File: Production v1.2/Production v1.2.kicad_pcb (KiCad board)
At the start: 2 copper layers, 35 x 31.2 mm, 39 parts, among them IC1 MAX3323EEUE+T, IC2 AP7375-33SA-7, J1 530480510, J13 FH34SRJ-16S-0.5SH_50_, J2 530480410, J3 USB4085-GF-A_REVB, U2 ADR02AUJZ-REEL7, U3 ATSAMD21G18A-AUT, Y1 ECS-.327-12.5-1210-TR

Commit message: 1.2 routed
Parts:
- removed 3V3, GND, SWCLK, SWDIO: TestPoint_Pad_D1.5mm, TestPoint:TestPoint_Pad_D1.5mm
- removed D4: LED, LED_SMD:LED_0805_2012Metric
- removed J13: FH34SRJ-16S-0.5SH_50_, FH34SRJ_16S_0_5SH_50:HRS_FH34SRJ-16S-0.5SH_50_
- added C14: 10uF, Capacitor_SMD:C_0402_1005Metric, B.Cu at (117.9, 89.2)
- added C15: 100nF, Capacitor_SMD:C_0402_1005Metric, B.Cu at (118.2, 85.7)
- added C16: 10uF, Capacitor_SMD:C_0402_1005Metric, B.Cu at (98.3, 82.2)
- added C17: 100nF, Capacitor_SMD:C_0402_1005Metric, B.Cu at (98.3, 84.1)
- added C18: 22uF,10V+, Capacitor_SMD:C_0402_1005Metric, B.Cu at (117.9, 87.4)
- added C19: 4.7uF, Capacitor_SMD:C_0402_1005Metric, B.Cu at (99.6, 83.3)
- added C20: 100nF, Capacitor_SMD:C_0402_1005Metric, B.Cu at (99.6, 85.2)
- added C21: 100nF, Capacitor_SMD:C_0402_1005Metric, B.Cu at (99.6, 84.3)
- added C22: .1uF, 10v+, Capacitor_SMD:C_0402_1005Metric, B.Cu at (92.5, 92.6)
- added C23: .1uF, 50V, Capacitor_SMD:C_0805_2012Metric, B.Cu at (95.3, 93.0)
- added C24: .1uF, 10v+, Capacitor_SMD:C_0402_1005Metric, B.Cu at (96.3, 86.5)
- added C25: .1uF, 50V, Capacitor_SMD:C_0805_2012Metric, B.Cu at (97.8, 90.9)
- added D3: D_Schottky, Diode_SMD:D_1206_3216Metric, B.Cu at (120.8, 92.3)
- added J4: FH34SRJ-16S-0.5SH_50_, FH34SRJ_16S_0_5SH_50:HRS_FH34SRJ-16S-0.5SH_50_, F.Cu at (106.5, 73.7)
- added L1: BLM15AX601SN1D, digikey-footprints:0603, B.Cu at (99.3, 81.2)
- added L2: BLM15AX601SN1D, digikey-footprints:0603, B.Cu at (100.6, 81.2)
- added R4: 5K6, Resistor_SMD:R_0201_0603Metric, B.Cu at (102.7, 88.2)
- added U1: ATSAMD21G18A-AUT, Package_QFP:TQFP-48_7x7mm_P0.5mm, B.Cu at (106.6, 81.8)
- C10, C11, C12, C9: moved to F.Cu
- C13: value 22uF,10V+ -> 2.2uF,50V+; footprint Capacitor_SMD:C_0402_1005Metric -> Capacitor_SMD:C_0805_2012Metric
- C4: value 2.2uF,100V -> 100nF,25V; footprint Capacitor_SMD:C_0805_2012Metric -> Capacitor_SMD:C_0402_1005Metric
- C5: value 100nF,25V -> 22pF
- C7: value 22pF -> 100nF
- C8: moved to B.Cu
- D1: value D_Schottky -> LED; footprint Diode_SMD:D_1206_3216Metric -> LED_SMD:LED_0805_2012Metric; moved to F.Cu
- R3: value 4K7 -> 65; moved to F.Cu
- R6: value 5K1 -> 1K
- R7: value 680K -> 5K1; moved to F.Cu
- R8: value 65 -> 680K
- U3: value ATSAMD21G18A-AUT -> ADR06BUJZ-REEL7; footprint Package_QFP:TQFP-48_7x7mm_P0.5mm -> Package_TO_SOT_SMD:TSOT-23-5
- moved D1 29.5 mm to (100.3, 69.1), turned to -90 degrees
- moved R6 17.4 mm to (105.7, 87.3)
- moved C7 15.1 mm to (111.0, 86.0), turned to -90 degrees
- moved U3 12.2 mm to (98.5, 88.0), turned to 90 degrees
- moved R5 11.2 mm to (104.3, 88.2), turned to 0 degrees
- moved Y1 11.2 mm to (101.6, 85.9), turned to 0 degrees
- moved C6 10.8 mm to (101.0, 84.0), turned to -90 degrees
- moved C5 10.8 mm to (103.0, 86.5), turned to 90 degrees
- moved C8 9.28 mm to (106.0, 88.2), turned to 180 degrees
- moved S1 8.73 mm to (90.7, 71.5), turned to 0 degrees
- moved C11 8.08 mm to (102.5, 76.6), turned to 180 degrees
- moved R7 7.76 mm to (112.5, 72.0)
- moved C4 7.29 mm to (112.8, 92.5)
- moved R3 6.86 mm to (99.9, 72.2)
- moved C13 6.84 mm to (119.0, 92.2)
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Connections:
- C13 pad 2: +3V3 -> VIN
- C4 pad 1: GND -> /Net-(IC1-V-)
- C4 pad 2: VIN -> GND
- C5 pad 1: /Net-(IC1-V-) -> GND
- C5 pad 2: GND -> Net-(U1-PA00)
- C6 pad 2: Net-(U3-PA00) -> Net-(U1-PA01)
- C7 pad 1: GND -> +3V3
- C7 pad 2: Net-(U3-PA01) -> GND
- C8 pad 1: Net-(U3-VDDCORE) -> VDDCORE
- D1 pad 1: VIN -> GND
- D1 pad 2: VUSB -> Net-(D1-A)
- D2 pad 2: +24V -> VUSB
- R3 pad 1: ZOOM -> SETLED
- R3 pad 2: ZSIG -> Net-(D1-A)
- R5 pad 2: GND -> GNDANA
- R6 pad 1: GND -> SWCLK
- R6 pad 2: OLED_RST -> +3V3
- R7 pad 2: Net-(J13-Pad4) -> OLED_RST
- R8 pad 1: SETLED -> GND
- U2 pad 2: GND -> GNDANA
- U2 pad 3: +24V -> VIN
- U3 pad 1: Net-(U3-PA00) -> unconnected-(U3-TEMP-Pad1)
- U3 pad 2: Net-(U3-PA01) -> GNDANA
- U3 pad 3: SETBTN -> VIN
- U3 pad 4: unconnected-(U3-PA03-Pad4) -> AREFA
- U3 pad 5: GND -> unconnected-(U3-TRIM-Pad5)
- Y1 pad 1: Net-(U3-PA01) -> Net-(U1-PA01)
- Y1 pad 2: Net-(U3-PA00) -> Net-(U1-PA00)
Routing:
- net VIN: track 0.00 -> 35.8 mm, vias 0 -> 2
- net GND: track 32.2 -> 0.00 mm, vias 23 -> 0
- net +3V3: track 33.0 -> 49.8 mm, vias 2 -> 1
- net AREFA: track 0.00 -> 13.3 mm
- net VUSB: track 24.8 -> 14.1 mm, vias 1 -> 0
- net SWCLK: track 11.4 -> 1.41 mm, vias 1 -> 0
- net SWDIO: track 9.92 -> 0.00 mm, vias 1 -> 0
- net SETBTN: track 8.41 -> 17.8 mm
- net VDDANA: track 0.00 -> 6.66 mm
- net SETLED: track 4.55 -> 10.3 mm
- net Net-(U3-PA00): track 4.92 -> 0.00 mm
- net OLED_RST: track 6.17 -> 10.9 mm, vias 2 -> 1
- net ZOOM: track 17.1 -> 12.5 mm
- net Net-(U3-PA01): track 4.04 -> 0.00 mm
- net D-: track 7.87 -> 11.9 mm, vias 0 -> 1
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- added copper zone on B.Cu, net GNDANA
- removed copper zone on B.Cu, net +3V3
- removed copper zone on B.Cu, net GND
- removed copper zone on F.Cu, net GND
- removed copper zone on B.Cu, net VIN
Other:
- outline, holes or cut-outs redrawn
- board text added: "MFSerial v1.2 Max Batchelder"
- board text removed: "MFSerial v1.1 Max Batchelder"

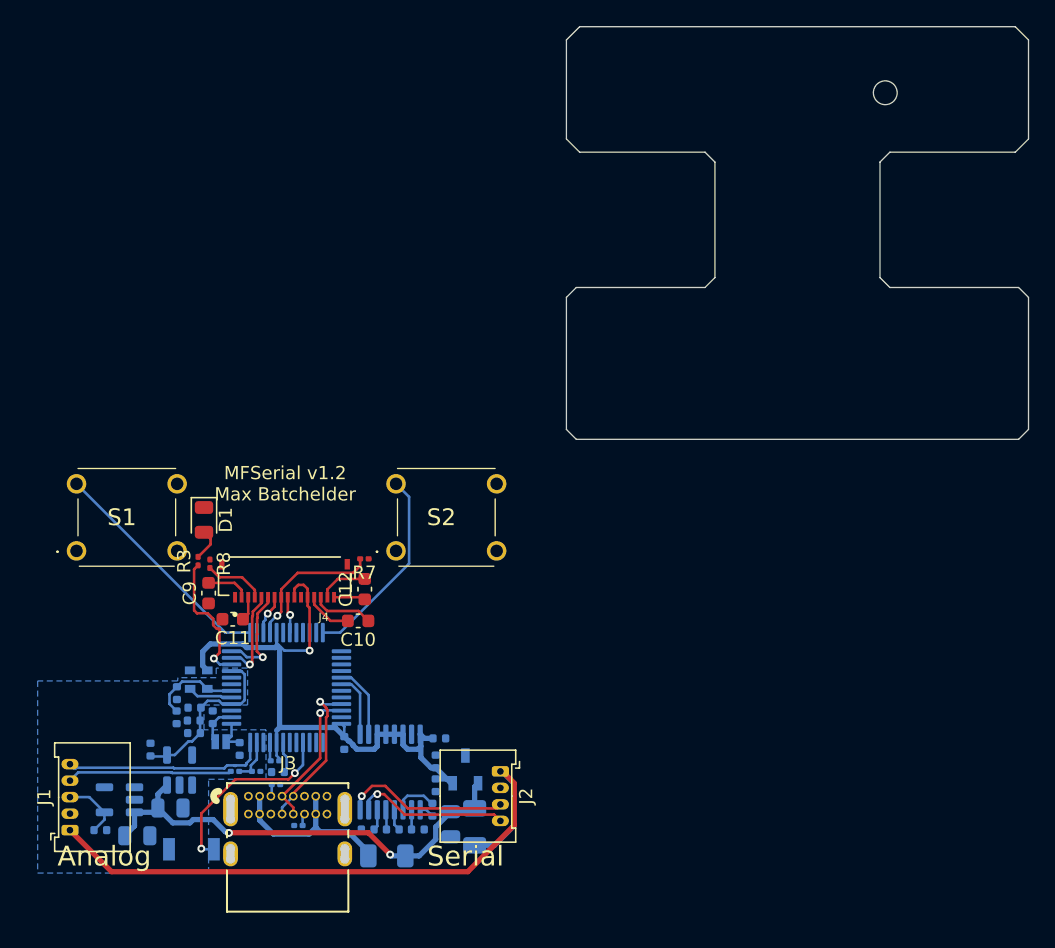
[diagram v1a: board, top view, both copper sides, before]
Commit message: v1.2 checked & labeled
flipped fpc connector to underside, for better ribbon routing.
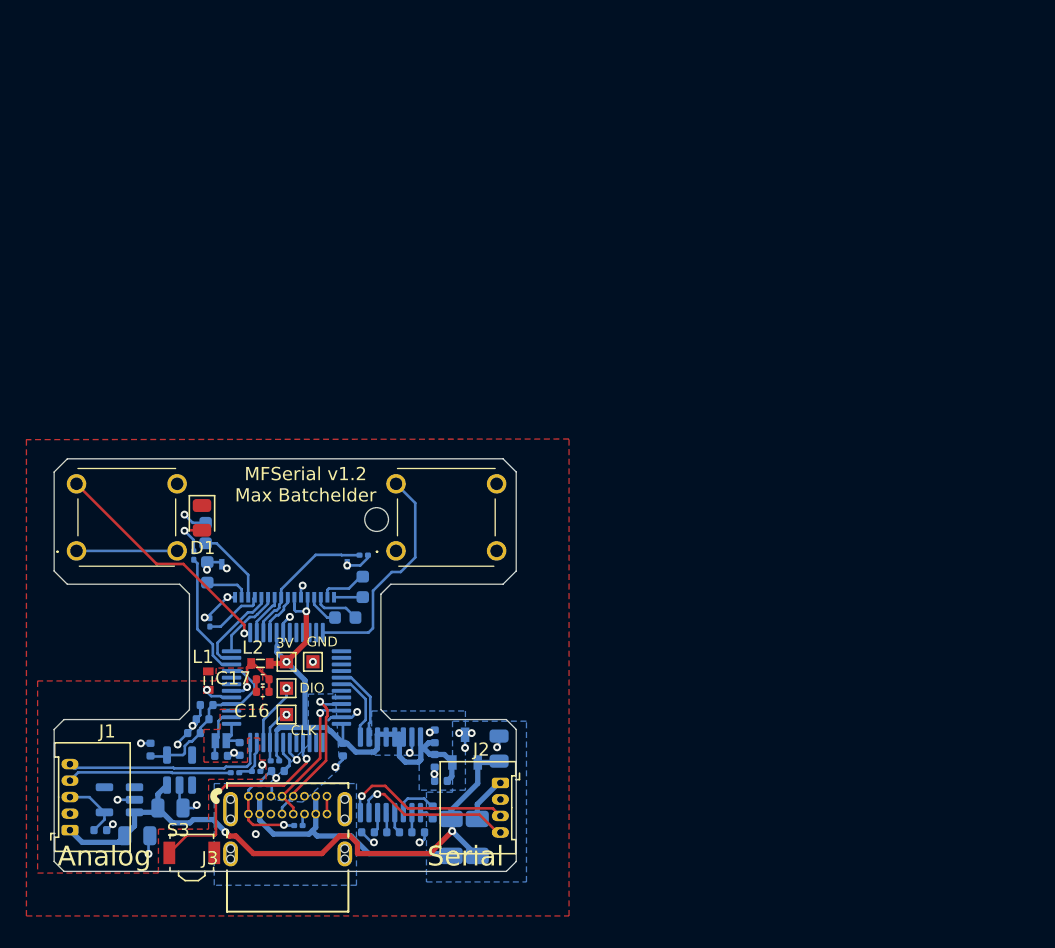
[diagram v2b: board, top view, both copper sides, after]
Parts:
- added TP1: 3V3, TestPoint:TestPoint_Pad_1.0x1.0mm, F.Cu at (106.6, 79.8)
- added TP2: GND, TestPoint:TestPoint_Pad_1.0x1.0mm, F.Cu at (108.6, 79.8)
- added TP3: SCK, TestPoint:TestPoint_Pad_1.0x1.0mm, F.Cu at (106.6, 83.8)
- added TP4: SWDIO, TestPoint:TestPoint_Pad_1.0x1.0mm, F.Cu at (106.6, 81.8)
- C10, C11, C12, C9, J4, R3, R7, R8: moved to B.Cu
- C16, C17, L1, L2, S3: moved to F.Cu
- moved C17 7.13 mm to (104.8, 81.2), turned to 180 degrees
- moved C11 6.84 mm to (100.5, 70.1), turned to 90 degrees
- moved C13 6.80 mm to (122.7, 86.4), turned to -90 degrees
- moved C16 6.50 mm to (104.8, 82.1), turned to 180 degrees
- moved D2 5.07 mm to (119.1, 93.2), turned to -90 degrees
- moved R8 4.44 mm to (100.8, 76.9)
- moved L2 4.21 mm to (104.6, 80.0), turned to 0 degrees
- moved C6 2.99 mm to (101.7, 87.0), turned to 180 degrees
- moved C9 1.58 mm to (100.6, 73.1), turned to -90 degrees
- moved U5 1.58 mm to (120.1, 86.4)
- moved L1 1.38 mm to (100.7, 81.3)
- moved C10 1.01 mm to (111.0, 76.5)
- moved C19 0.95 mm to (100.5, 83.1)
- moved R1 0.90 mm to (104.9, 89.2), turned to 0 degrees
- moved J2 0.88 mm to (122.8, 89.0)
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- renumbered IC1 to U4, IC2 to U5
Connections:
- J1 pad 1: +24V -> VIN
- J1 pad 2: GND -> GNDANA
- J4 pad 1: GND -> Net-(C12-Pad1)
- J4 pad 10: +3V3 -> OLED_DC
- J4 pad 11: GND -> SCK
- J4 pad 12: +3V3 -> MOSI
- J4 pad 13: Net-(C10-Pad2) -> Net-(J4-Pad13)
- J4 pad 14: Net-(C10-Pad1) -> Net-(C11-Pad1)
- J4 pad 15: Net-(C12-Pad2) -> Net-(C9-Pad2)
- J4 pad 16: Net-(C12-Pad1) -> GND
- J4 pad 2: Net-(C9-Pad2) -> Net-(C12-Pad2)
- J4 pad 3: Net-(C11-Pad1) -> Net-(C10-Pad1)
- J4 pad 4: Net-(J4-Pad4) -> Net-(C10-Pad2)
- J4 pad 5: MOSI -> +3V3
- J4 pad 6: SCK -> GND
- J4 pad 7: OLED_DC -> +3V3
- J4 pad 8: OLED_RST -> OLED_CS
- J4 pad 9: OLED_CS -> OLED_RST
- R8 pad 2: Net-(J4-Pad4) -> Net-(J4-Pad13)
- U1 pad 14: unconnected-(U1-PA09-Pad14) -> OLED_DC
- U1 pad 15: OLED_DC -> OLED_RST
- U1 pad 16: OLED_RST -> OLED_CS
- U1 pad 19: OLED_CS -> unconnected-(U1-PB10-Pad19)
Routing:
- net +24V: track 49.2 -> 3.53 mm
- net GND: track 0.00 -> 42.5 mm, vias 0 -> 25
- net GNDANA: track 3.41 -> 15.1 mm, vias 0 -> 9
- net VIN: track 35.8 -> 47.3 mm
- net +3V3: track 49.8 -> 42.2 mm, vias 1 -> 2
- net VUSB: track 14.1 -> 20.4 mm
- net SWDIO: track 0.00 -> 4.84 mm, vias 0 -> 1
- net Net-(J4-Pad4): track 4.64 -> 0.00 mm
- net Net-(J4-Pad13): track 0.00 -> 4.61 mm
- net Net-(C11-Pad1): track 1.83 -> 5.91 mm
- net SWCLK: track 1.41 -> 4.19 mm, vias 0 -> 1
- net SCK: track 7.62 -> 5.48 mm, vias 1 -> 0
- net RST: track 14.6 -> 16.6 mm, vias 2 -> 1
- net SOFTBTN: track 15.2 -> 17.2 mm
- net Net-(C10-Pad2): track 3.62 -> 2.54 mm
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- added copper zone on B.Cu, net +3V3
- added copper zone on B.Cu, net GND
- added copper zone on F.Cu, net GND
- added copper zone on F.Cu, net GNDANA
- added copper zone on B.Cu, net VIN
- removed copper zone on B.Cu, net GNDANA
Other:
- outline, holes or cut-outs redrawn
- board text added: "3V"
- board text added: "CLK"
- board text added: "DIO"
- board text added: "GND"

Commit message: Updated some fields
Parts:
- moved L1 0.08 mm to (100.6, 81.2)
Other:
- outline, holes or cut-outs redrawn
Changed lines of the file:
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@@
 		(sheetname "Root")
 		(sheetfile "Production v1.2.kicad_sch")
-		(attr exclude_from_pos_files)
+		(attr exclude_from_pos_files dnp)
 		(fp_line
 			(start -0.7 -0.7)
@@
 		(sheetname "Root")
 		(sheetfile "Production v1.2.kicad_sch")
-		(attr exclude_from_pos_files)
+		(attr exclude_from_pos_files dnp)
 		(fp_line
 			(start -0.7 -0.7)
@@
 		(sheetname "Root")
 		(sheetfile "Production v1.2.kicad_sch")
-		(attr exclude_from_pos_files)
+		(attr exclude_from_pos_files dnp)
 		(fp_line
 			(start -0.7 -0.7)
@@
 	(footprint "digikey-footprints:0603"
 		(layer "F.Cu")
-		(at 100.675 81.275 90)
+		(at 100.6 81.25 90)
 		(property "Reference" "L1"
 			(at 1.8 -0.4 0)
@@
 			)
 		)
+		(property "Part Number" "BLM15AX601SN1D"
+			(at 0 0 90)
+			(unlocked yes)
+			(layer "F.Fab")
+			(hide yes)
+			(effects
+				(font
+					(size 1 1)
+					(thickness 0.15)
+				)
+			)
+		)
+		(property "URL" "https://www.digikey.com/en/products/detail/murata-electronics/BLM15AX601SN1D/2256876?s=N4IgTCBcDaIEIBkCyBGArAQQBoDYAMKAygHIoAiIAugL5A"
+			(at 0 0 90)
+			(unlocked yes)
+			(layer "F.Fab")
+			(hide yes)
+			(effects
+				(font
+					(size 1 1)
+					(thickness 0.15)
+				)
+			)
+		)
 		(sheetname "Root")
 		(sheetfile "Production v1.2.kicad_sch")
@@
 			)
 		)
+		(property "Part Number" "BLM15AX601SN1D"
+			(at 0 0 0)
+			(unlocked yes)
+			(layer "F.Fab")
+			(hide yes)
+			(effects
+				(font
+					(size 1 1)
+					(thickness 0.15)
+				)
+			)
+		)
+		(property "URL" "https://www.digikey.com/en/products/detail/murata-electronics/BLM15AX601SN1D/2256876?s=N4IgTCBcDaIEIBkCyBGArAQQBoDYAMKAygHIoAiIAugL5A"
+			(at 0 0 0)
+			(unlocked yes)
+			(layer "F.Fab")
+			(hide yes)
+			(effects
+				(font
+					(size 1 1)
+					(thickness 0.15)
+				)
+			)
+		)
 		(sheetname "Root")
 		(sheetfile "Production v1.2.kicad_sch")
@@
 		(sheetname "Root")
 		(sheetfile "Production v1.2.kicad_sch")
-		(attr exclude_from_pos_files)
+		(attr exclude_from_pos_files dnp)
 		(fp_line
 			(start -0.7 -0.7)
@@
 		(tags "capacitor")
 		(property "Reference" "C11"
-			(at 3.225 0.525 0)
+			(at 2.3 2.025 0)
 			(layer "B.SilkS")
 			(effects
@@
 			)
 		)
+		(property "Part Number" "ECS-.327-12.5-1210-TR"
+			(at 0 0 0)
+			(unlocked yes)
+			(layer "B.Fab")
+			(hide yes)
+			(effects
+				(font
+					(size 1 1)
+					(thickness 0.15)
+				)
+				(justify mirror)
+			)
+		)
+		(property "URL" "https://www.digikey.com/en/products/detail/ecs-inc/ECS-327-12-5-1210-TR/6821602?s=N4IgTCBcDaIKIGEDKBaAdAZjAdhQRjDQFZ8w8AGFAFQCUQBdAXyA"
+			(at 0 0 0)
+			(unlocked yes)
+			(layer "B.Fab")
+			(hide yes)
+			(effects
+				(font
+					(size 1 1)
+					(thickness 0.15)
+				)
+				(justify mirror)
+			)
+		)
 		(sheetname "Root")
 		(sheetfile "Production v1.2.kicad_sch")
@@
 	)
 	(gr_line
+		(start 101 66.3)
+		(end 111.8 66.3)
+		(stroke
+			(width 0.05)
+			(type default)
+		)
+		(layer "Edge.Cuts")
+	)
+	(gr_line
 		(start 99.25 83.475)
 		(end 99.25 74.725)
@@
 	)
 	(gr_line
+		(start 123 64.475)
+		(end 113.499967 64.475)
+		(stroke
+			(width 0.05)
+			(type default)
+		)
+		(layer "Edge.Cuts")
+	)
+	(gr_line
 		(start 123.25 95.725)
 		(end 89.75 95.725)
@@
 	)
 	(gr_line
+		(start 90 64.475)
+		(end 99.5 64.5)
+		(stroke
+			(width 0.05)
+			(type default)
+		)
+		(layer "Edge.Cuts")
+	)
+	(gr_line
 		(start 89.75 95.725)
 		(end 89 94.975)
@@
 	)
 	(gr_line
-		(start 90 64.475)
-		(end 123 64.475)
+		(start 113.499967 64.475)
+		(end 111.8 66.3)
 		(stroke
 			(width 0.05)
@@
 		(layer "Edge.Cuts")
 	)
+	(gr_line
+		(start 99.5 64.5)
+		(end 101 66.3)
+		(stroke
+			(width 0.05)
+			(type default)
+		)
+		(layer "Edge.Cuts")
+	)
 	(gr_text "MFSerial v1.2\nMax Batchelder"
-		(at 108.05 67.825 0)
-		(layer "F.SilkS")
+		(at 106.934 70.612 -0)
+		(layer "B.SilkS")
 		(effects
 			(font
@@
 				(thickness 0.15)
 			)
-			(justify bottom)
+			(justify bottom mirror)
 		)
 	)

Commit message: Final tweaks for production v1.2, as manufactured
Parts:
- C13: value 2.2uF,50V+ -> 2.2uF,100V
- C23, C25: value .1uF, 50V -> .1uF, 100V
- L1: value BLM15AX601SN1D -> 600 MHz @ 100 MHz
- L2: value BLM15AX601SN1D -> 600 Ohm @ 100 MHz
- R4, R5: footprint Resistor_SMD:R_0201_0603Metric -> Resistor_SMD:R_0402_1005Metric
- moved R4 1.03 mm to (101.7, 88.2)
- moved R5 0.67 mm to (103.6, 88.2)
- moved C20 0.43 mm to (99.2, 85.5)
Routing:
- net GNDANA: track 15.1 -> 17.5 mm
- net +3V3: track 42.2 -> 44.6 mm
- net GND: track 42.5 -> 44.1 mm, vias 25 -> 24
- net ZOOM: track 12.5 -> 11.2 mm
- net ZSIG: track 3.34 -> 3.91 mm
